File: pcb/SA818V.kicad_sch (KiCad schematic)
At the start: 45 parts, among them J6 SJ2-3593D-SMT-TR, J8 RF_SMA, Q12 BSS138, Q13 BSS138, Q14 BSS138, U20 SA818S-V, U21 74HC123, U23 74LVC1G38, U24 74LVC1G38

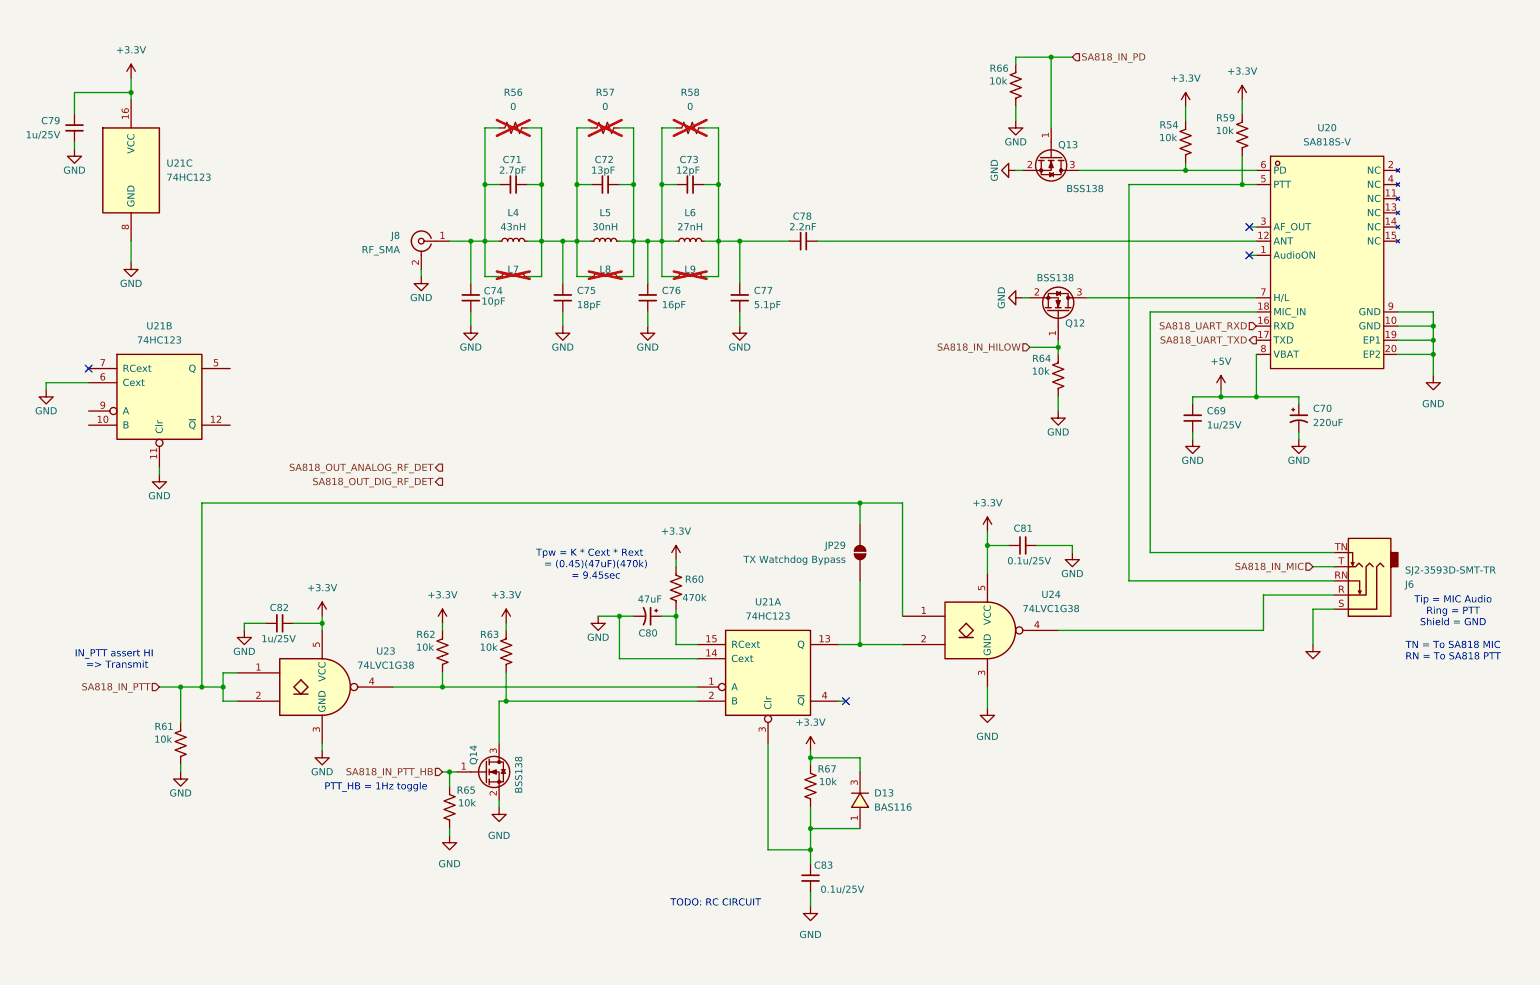
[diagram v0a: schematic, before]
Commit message: audio path
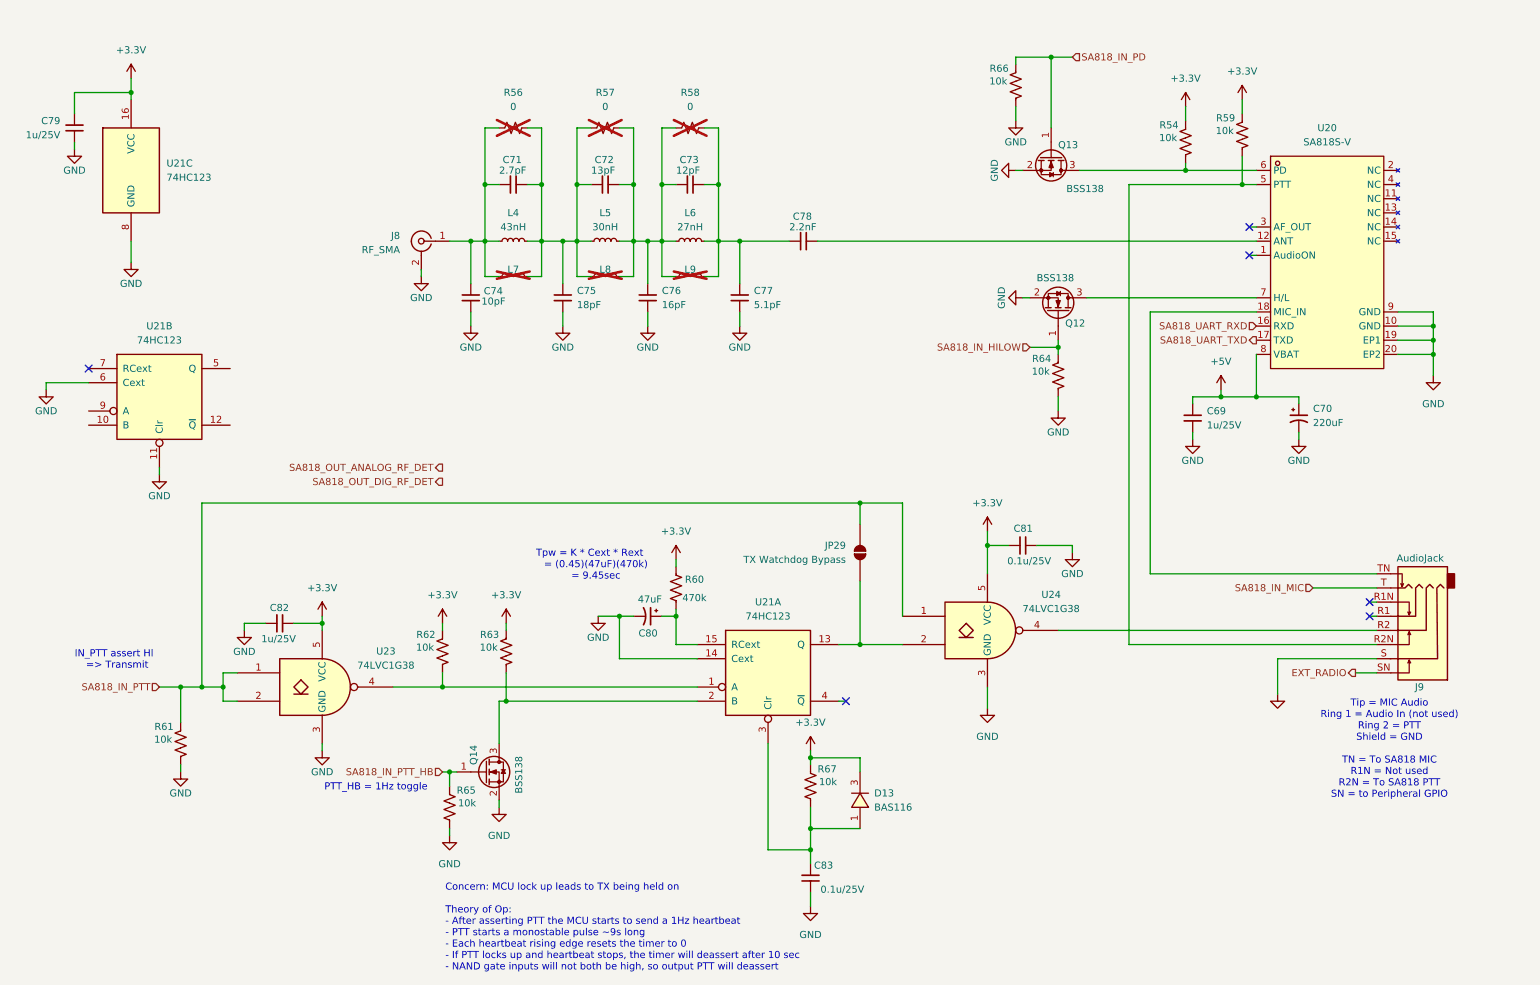
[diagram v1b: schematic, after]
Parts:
- removed J6: SJ2-3593D-SMT-TR, Connector_Audio:Jack_3.5mm_CUI_SJ2-3593D-SMT_Horizontal, symbol Connector_Audio:AudioJack3_SwitchTR
- added J9: AudioJack, kicad_gx_library:Jack_SJ-43617-SMT-TR, symbol kicad_gx_library:AudioJack4_TRRS_SJ-43617-SMT-TR
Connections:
- net GND: now also J9.S
- net SA818_IN_MIC: now also J9.T
- net at U20.18 (MIC_IN): now also J9.TN
- net at R59.1, U20.5 (PTT): now also J9.R2N
- net at U24.4: now also J9.R2
- new net EXT_RADIO: J9.SN
- no-connect marks 4 -> 6
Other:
- note added: "Concern: MCU lock up leads to TX being held on Theory of Op: - After asserting PTT the MCU starts to send a 1Hz heartbeat - PTT starts a monostable pulse ~9s long - Each heartbeat rising edge resets the timer to 0 - If PTT locks up and heartbeat stops, the timer will deassert after 10 sec - NAND gate inputs will not both be high, so output PTT will deassert"
- note added: "Tip = MIC Audio Ring 1 = Audio In (not used) Ring 2 = PTT Shield = GND TN = To SA818 MIC R1N = Not used R2N = To SA818 PTT SN = to Peripheral GPIO"
- note removed: "TODO: RC CIRCUIT"
- note removed: "Tip = MIC Audio Ring = PTT Shield = GND TN = To SA818 MIC RN = To SA818 PTT"

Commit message: annotations
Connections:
- no-connect marks 6 -> 10
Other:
- note added: "EXTERNAL RADIO"
- note added: "PTT TX LOCKUP WATCHDOG"
- note added: "RADIO"
- moved on the sheet: C79, U21C
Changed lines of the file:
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@@
 		)
 	)
+	(text "EXTERNAL\nRADIO"
+		(exclude_from_sim no)
+		(at 264.922 103.886 0)
+		(effects
+			(font
+				(size 3.81 3.81)
+			)
+		)
+	)
 	(text "Tpw = K * Cext * Rext\n    = (0.45)(47uF)(470k)\n    = 9.45sec"
 		(exclude_from_sim no)
@@
 		)
 	)
+	(text "RADIO"
+		(exclude_from_sim no)
+		(at 22.352 16.256 0)
+		(effects
+			(font
+				(size 3.81 3.81)
+			)
+		)
+	)
+	(text "PTT TX LOCKUP WATCHDOG"
+		(exclude_from_sim no)
+		(at 102.87 95.758 0)
+		(effects
+			(font
+				(size 3.81 3.81)
+			)
+		)
+	)
 	(text "Concern: MCU lock up leads to TX being held on\n\nTheory of Op:\n- After asserting PTT the MCU starts to send a 1Hz heartbeat\n- PTT starts a monostable pulse ~9s long\n- Each heartbeat rising edge resets the timer to 0\n- If PTT locks up and heartbeat stops, the timer will deassert after 10 sec\n- NAND gate inputs will not both be high, so output PTT will deassert"
 		(exclude_from_sim no)
@@
 	)
 	(junction
-		(at 33.02 26.67)
+		(at 49.53 33.02)
 		(diameter 0)
 		(color 0 0 0 0)
@@
 	)
 	(no_connect
+		(at 25.4 83.82)
+	)
+	(no_connect
+		(at 50.8 86.36)
+	)
+	(no_connect
 		(at 161.29 135.89)
 	)
@@
 	)
 	(no_connect
+		(at 25.4 86.36)
+	)
+	(no_connect
 		(at 255.27 118.11)
 	)
 	(no_connect
+		(at 50.8 76.2)
+	)
+	(no_connect
 		(at 233.68 50.8)
 	)
@@
 	(wire
 		(pts
-			(xy 33.02 53.34) (xy 33.02 57.15)
+			(xy 49.53 59.69) (xy 49.53 63.5)
 		)
 		(stroke
@@
 	(wire
 		(pts
-			(xy 33.02 26.67) (xy 33.02 27.94)
+			(xy 49.53 33.02) (xy 49.53 34.29)
 		)
 		(stroke
@@
 	(wire
 		(pts
-			(xy 33.02 24.13) (xy 33.02 26.67)
+			(xy 49.53 30.48) (xy 49.53 33.02)
 		)
 		(stroke
@@
 	(wire
 		(pts
-			(xy 22.86 30.48) (xy 22.86 26.67)
+			(xy 39.37 36.83) (xy 39.37 33.02)
 		)
 		(stroke
@@
 	(wire
 		(pts
-			(xy 22.86 26.67) (xy 33.02 26.67)
+			(xy 39.37 33.02) (xy 49.53 33.02)
 		)
 		(stroke
@@
 	(wire
 		(pts
-			(xy 22.86 35.56) (xy 22.86 36.83)
+			(xy 39.37 41.91) (xy 39.37 43.18)
 		)
 		(stroke
@@
 		)
 	)
-	(hierarchical_label "SA818_OUT_ANALOG_RF_DET"
-		(shape output)
-		(at 88.9 93.98 180)
-		(effects
-			(font
-				(size 1.27 1.27)
-			)
-			(justify right)
-		)
-	)
 	(hierarchical_label "SA818_IN_PTT_HB"
 		(shape input)
@@
 		)
 	)
-	(hierarchical_label "SA818_OUT_DIG_RF_DET"
-		(shape output)
-		(at 88.9 96.52 180)
-		(effects
-			(font
-				(size 1.27 1.27)
-			)
-			(justify right)
-		)
-	)
 	(symbol
 		(lib_id "kicad_gx_library:BAS116LT1G")
@@
 	(symbol
 		(lib_id "power:+3.3V")
-		(at 33.02 24.13 0)
+		(at 49.53 30.48 0)
 		(unit 1)
 		(body_style 1)
@@
 		(fields_autoplaced yes)
 		(property "Reference" "#PWR0169"
-			(at 33.02 27.94 0)
+			(at 49.53 34.29 0)
 			(hide yes)
 			(show_name no)
@@
 		)
 		(property "Value" "+3.3V"
-			(at 33.02 19.05 0)
+			(at 49.53 25.4 0)
 			(show_name no)
 			(do_not_autoplace no)
@@
 		)
 		(property "Footprint" ""
-			(at 33.02 24.13 0)
+			(at 49.53 30.48 0)
 			(hide yes)
 			(show_name no)
@@
 		)
 		(property "Datasheet" ""
-			(at 33.02 24.13 0)
+			(at 49.53 30.48 0)
 			(hide yes)
 			(show_name no)
@@
 		)
 		(property "Description" "Power symbol creates a global label with name \"+3.3V\""
-			(at 33.02 24.13 0)
+			(at 49.53 30.48 0)
 			(hide yes)
 			(show_name no)
@@
 	(symbol
 		(lib_id "74xx:74HC123")
-		(at 33.02 40.64 0)
+		(at 49.53 46.99 0)
 		(unit 3)
 		(body_style 1)
@@
 		(fields_autoplaced yes)
 		(property "Reference" "U21"
-			(at 39.37 39.3699 0)
+			(at 55.88 45.7199 0)
 			(show_name no)
 			(do_not_autoplace no)
@@
 		)
 		(property "Value" "74HC123"
-			(at 39.37 41.9099 0)
+			(at 55.88 48.2599 0)
 			(show_name no)
 			(do_not_autoplace no)
@@
 		)
 		(property "Footprint" "Package_SO:SOIC-16_3.9x9.9mm_P1.27mm"
-			(at 33.02 40.64 0)
+			(at 49.53 46.99 0)
 			(hide yes)
 			(show_name no)
@@
 		)
 		(property "Datasheet" "https://assets.nexperia.com/documents/data-sheet/74HC_HCT123.pdf"
-			(at 33.02 40.64 0)
+			(at 49.53 46.99 0)
 			(hide yes)
 			(show_name no)
@@
 		)
 		(property "Description" "Dual retriggerable monostable multivibrator with reset"
-			(at 33.02 40.64 0)
+			(at 49.53 46.99 0)
 			(hide yes)
 			(show_name no)
@@
 		)
 		(property "Manf" "Nexperia"
-			(at 33.02 40.64 0)
+			(at 49.53 46.99 0)
 			(hide yes)
 			(show_name no)
@@
 		)
 		(property "MPN" "74HC123D,653"
-			(at 33.02 40.64 0)
+			(at 49.53 46.99 0)
 			(hide yes)
 			(show_name no)
@@
 		)
 		(property "LCSC Part #" "C5597"
-			(at 33.02 40.64 0)
+			(at 49.53 46.99 0)
 			(hide yes)
 			(show_name no)
@@
 		)
 		(property "Package" "SOIC-16"
-			(at 33.02 40.64 0)
+			(at 49.53 46.99 0)
 			(hide yes)
 			(show_name no)
@@
 	(symbol
 		(lib_id "Device:C_Small")
-		(at 22.86 33.02 0)
+		(at 39.37 39.37 0)
 		(mirror y)
 		(unit 1)
@@
 		(fields_autoplaced yes)
 		(property "Reference" "C79"
-			(at 20.32 31.7499 0)
+			(at 36.83 38.0999 0)
 			(show_name no)
 			(do_not_autoplace no)
@@
 		)
 		(property "Value" "1u/25V"
-			(at 20.32 34.2899 0)
+			(at 36.83 40.6399 0)
 			(show_name no)
 			(do_not_autoplace no)
@@
 		)
 		(property "Footprint" "Capacitor_SMD:C_0805_2012Metric"
-			(at 22.86 33.02 0)
+			(at 39.37 39.37 0)
 			(hide yes)
 			(show_name no)
@@
 		)
 		(property "Datasheet" "${KIPRJMOD}/project_library/datasheets/Murata_Electronics/GRM21BR71H105KA12L.pdf"
-			(at 22.86 33.02 0)
+			(at 39.37 39.37 0)
 			(hide yes)
 			(show_name no)
@@
 		)
 		(property "Description" "Unpolarized capacitor, small symbol"
-			(at 22.86 43.18 0)
+			(at 39.37 49.53 0)
 			(hide yes)
 			(show_name no)
@@
 		)
 		(property "Manf" "muRata"
-			(at 22.86 33.02 0)
+			(at 39.37 39.37 0)
 			(hide yes)
 			(show_name no)
@@
 		)
 		(property "MPN" "GRM21BR71H105KA12L"
-			(at 22.86 33.02 0)
+			(at 39.37 39.37 0)
 			(hide yes)
 			(show_name no)
@@
 		)
 		(property "LCSC Part #" "C77083"
-			(at 22.86 33.02 0)
+			(at 39.37 39.37 0)
 			(hide yes)
 			(show_name no)
@@
 		)
 		(property "Package" "0805"
-			(at 22.86 33.02 0)
+			(at 39.37 39.37 0)
 			(hide yes)
 			(show_name no)
@@
 		)
 		(property "Field10" ""
-			(at 22.86 33.02 0)
+			(at 39.37 39.37 0)
 			(hide yes)
 			(show_name no)
@@
 	(symbol
 		(lib_id "PCM_SparkFun-PowerSymbol:GND")
-		(at 22.86 36.83 0)
+		(at 39.37 43.18 0)
 		(mirror y)
 		(unit 1)
@@
 		(fields_autoplaced yes)
 		(property "Reference" "#PWR0171"
-			(at 22.86 43.18 0)
+			(at 39.37 49.53 0)
 			(hide yes)
 			(show_name no)
@@
 		)
 		(property "Value" "GND"
-			(at 22.86 40.64 0)
+			(at 39.37 46.99 0)
 			(show_name no)
 			(do_not_autoplace yes)
@@
 		)
 		(property "Footprint" ""
-			(at 22.86 36.83 0)
+			(at 39.37 43.18 0)
 			(hide yes)
 			(show_name no)
@@
 		)
 		(property "Datasheet" ""
-			(at 22.86 36.83 0)
+			(at 39.37 43.18 0)
 			(hide yes)
 			(show_name no)
@@
 		)
 		(property "Description" "Power symbol creates a global label with name \"GND\" , ground"
-			(at 22.86 45.72 0)
+			(at 39.37 52.07 0)
 			(hide yes)
 			(show_name no)
@@
 	(symbol
 		(lib_id "PCM_SparkFun-PowerSymbol:GND")
-		(at 33.02 57.15 0)
+		(at 49.53 63.5 0)
 		(mirror y)
 		(unit 1)
@@
 		(fields_autoplaced yes)
 		(property "Reference" "#PWR0170"
-			(at 33.02 63.5 0)
+			(at 49.53 69.85 0)
 			(hide yes)
 			(show_name no)
@@
 		)
 		(property "Value" "GND"
-			(at 33.02 60.96 0)
+			(at 49.53 67.31 0)
 			(show_name no)
 			(do_not_autoplace yes)
@@
 		)
 		(property "Footprint" ""
-			(at 33.02 57.15 0)
+			(at 49.53 63.5 0)
 			(hide yes)
 			(show_name no)
@@
 		)
 		(property "Datasheet" ""
-			(at 33.02 57.15 0)
+			(at 49.53 63.5 0)
 			(hide yes)
 			(show_name no)
@@
 		)
 		(property "Description" "Power symbol creates a global label with name \"GND\" , ground"
-			(at 33.02 66.04 0)
+			(at 49.53 72.39 0)
 			(hide yes)
 			(show_name no)

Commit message: changes on pcb
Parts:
- R56, R57, R58: footprint Resistor_THT:R_Array_SIP4 -> Resistor_SMD:R_0603_1608Metric
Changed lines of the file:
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@@
 			)
 		)
-		(property "Footprint" "Resistor_THT:R_Array_SIP4"
+		(property "Footprint" "Resistor_SMD:R_0603_1608Metric"
 			(at 133.35 33.02 0)
 			(hide yes)
@@
 			)
 		)
-		(property "Footprint" "Resistor_THT:R_Array_SIP4"
+		(property "Footprint" "Resistor_SMD:R_0603_1608Metric"
 			(at 118.11 33.02 0)
 			(hide yes)
@@
 			)
 		)
-		(property "Footprint" "Resistor_THT:R_Array_SIP4"
+		(property "Footprint" "Resistor_SMD:R_0603_1608Metric"
 			(at 101.6 33.02 0)
 			(hide yes)
